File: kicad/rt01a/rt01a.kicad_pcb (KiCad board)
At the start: 4 copper layers, 90 x 66.3 mm, 75 parts, among them J1 Barrel_Jack_Switch, J10 Conn_01x07, J2 USB_C_Receptacle_USB2.0_14P, J3 Conn_01x07, J4 Conn_01x12, J5 Conn_01x12, J6 Conn_01x06, J7 Conn_01x02, J8 Conn_01x05, J9 Conn_01x04, Q1 DMP3099L, U1 R-78E5.0-1.0, U2 MCP73831-2-OT, U3 TLV75533PDBV, U4 MCP111T-xxxE_TT, U5 STM32L412R8Tx, U6 AT25SF081-SSHD-X, U7 RV-3028-C7

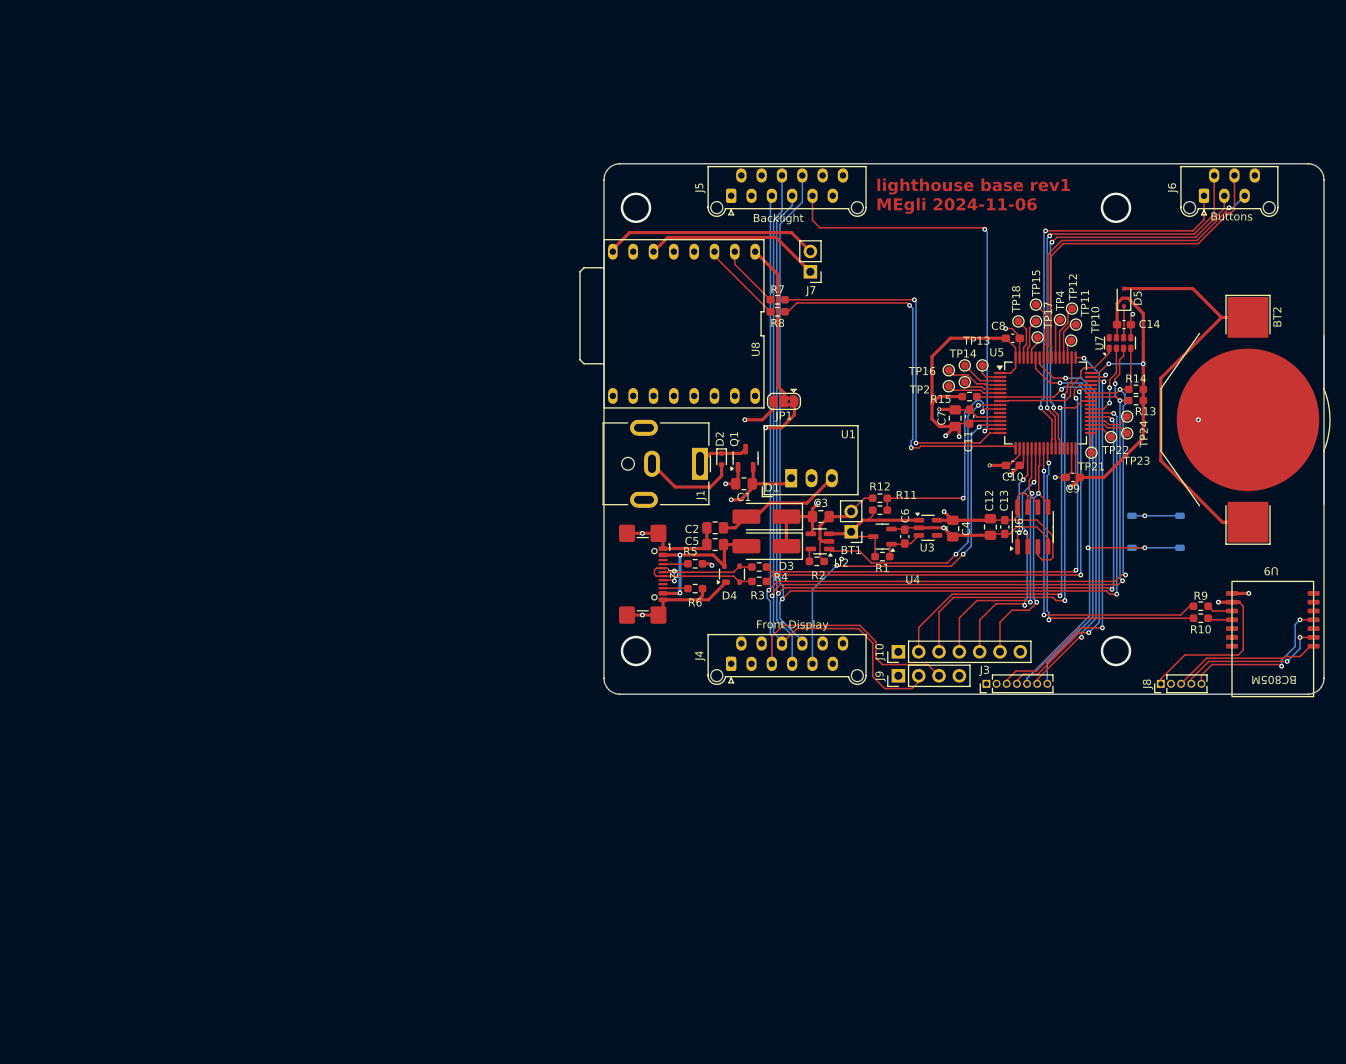
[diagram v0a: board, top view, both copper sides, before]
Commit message: rt01a added footprint, some placements done
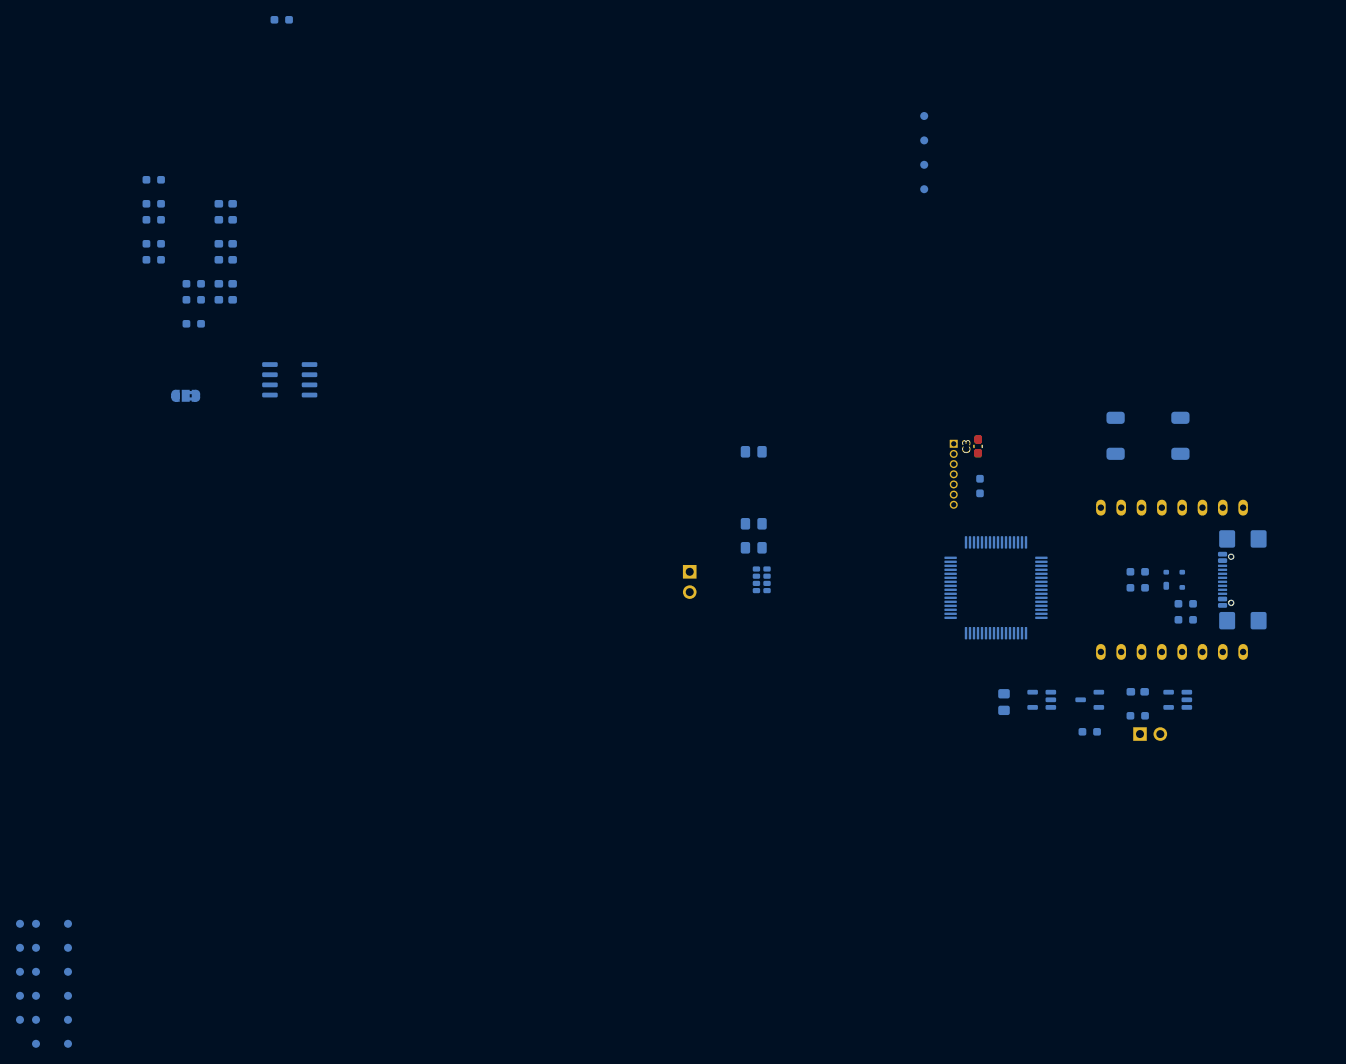
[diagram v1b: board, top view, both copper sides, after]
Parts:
- removed BT2: Keystone 3002, Battery:BatteryHolder_Keystone_3002_1x2032
- removed C13, C14: 100nF, Capacitor_SMD:C_0603_1608Metric_Pad1.08x0.95mm_HandSolder
- removed D2: DF2S16FS, Diode_SMD:D_SOD-523
- removed D3: B130-13-F, Diode_SMD:D_SMA_Handsoldering
- removed D4: PRTR5V0U2X, Package_TO_SOT_SMD:SOT-143
- removed D5: PMEG4002EJ, Diode_SMD:D_SOD-323F
- removed J10: Conn_01x07, Connector_PinHeader_2.54mm:PinHeader_1x07_P2.54mm_Vertical
- removed J2: USB_C_Receptacle_USB2.0_14P, Connector_USB:USB_C_Receptacle_GCT_USB4110
- removed J3: Conn_01x07, Connector_PinHeader_1.27mm:PinHeader_1x07_P1.27mm_Vertical
- removed J6: Conn_01x06, Connector_Molex:Molex_Picoflex_90325-0006_2x03_P1.27mm_Vertical
- removed J7: Conn_01x02, Connector_PinHeader_2.54mm:PinHeader_1x02_P2.54mm_Vertical
- removed J8: Conn_01x05, Connector_PinHeader_1.27mm:PinHeader_1x05_P1.27mm_Vertical
- removed J9: Conn_01x04, Connector_PinHeader_2.54mm:PinHeader_1x04_P2.54mm_Vertical
- removed Q1: DMP3099L, Package_TO_SOT_SMD:SOT-23-3
- removed TP22, TP23, TP24: TestPoint, TestPoint:TestPoint_Pad_D1.0mm
- removed U8: ~, lighthouse:DFPlayer_Mini-TF-16P
- removed U9: ~, lighthouse:BC805M
- added R16: 10k, Resistor_SMD:R_0603_1608Metric_Pad0.98x0.95mm_HandSolder, B.Cu at (-0.28, 30.0)
- added TP19: TestPoint, TestPoint:TestPoint_Pad_D1.0mm, B.Cu at (80.0, 45.1)
- added TP20: TestPoint, TestPoint:TestPoint_Pad_D1.0mm, B.Cu at (80.0, 48.1)
- added TP5: TestPoint, TestPoint:TestPoint_Pad_D1.0mm, B.Cu at (-27.0, 155.0)
- added TP6: TestPoint, TestPoint:TestPoint_Pad_D1.0mm, B.Cu at (-27.0, 158.0)
- added TP7: TestPoint, TestPoint:TestPoint_Pad_D1.0mm, B.Cu at (-31.0, 143.0)
- added TP8: TestPoint, TestPoint:TestPoint_Pad_D1.0mm, B.Cu at (-31.0, 146.0)
- added TP9: TestPoint, TestPoint:TestPoint_Pad_D1.0mm, B.Cu at (-31.0, 149.0)
- BT1, C1, C10, C2, C5, C8, C9, JP1, R1, R11, R12, R15, R2, R3, R4, R5, R6, R7, R8, TP1, TP10, TP11, TP12, TP13, TP14, TP15, TP16, TP17, TP18, TP2, TP21, TP3, TP4, U6, U7: moved to B.Cu
- C11: value 100nF -> 10uF; footprint Capacitor_SMD:C_0603_1608Metric_Pad1.08x0.95mm_HandSolder -> Capacitor_SMD:C_0805_2012Metric_Pad1.18x1.45mm_HandSolder; moved to B.Cu
- C12, C7: value 10uF -> 100nF; footprint Capacitor_SMD:C_0805_2012Metric_Pad1.18x1.45mm_HandSolder -> Capacitor_SMD:C_0603_1608Metric_Pad1.08x0.95mm_HandSolder; moved to B.Cu
- C3: value 10uF -> 10nF; footprint Capacitor_SMD:C_0805_2012Metric_Pad1.18x1.45mm_HandSolder -> Capacitor_SMD:C_0603_1608Metric_Pad1.08x0.95mm_HandSolder
- C4: value 10uF -> 10nF; footprint Capacitor_SMD:C_0805_2012Metric_Pad1.18x1.45mm_HandSolder -> Capacitor_SMD:C_0603_1608Metric_Pad1.08x0.95mm_HandSolder; moved to B.Cu
- C6: value 10nF -> 100nF; moved to B.Cu
- D1: value B130-13-F -> PRTR5V0U2X; footprint Diode_SMD:D_SMA_Handsoldering -> Package_TO_SOT_SMD:SOT-143; moved to B.Cu
- J1: value Barrel_Jack_Switch -> USB_C_Receptacle_USB2.0_14P; footprint Connector_BarrelJack:BarrelJack_CUI_PJ-063AH_Horizontal -> Connector_USB:USB_C_Receptacle_GCT_USB4110; moved to B.Cu
- J4: value Conn_01x12 -> Conn_01x07; footprint Connector_Molex:Molex_Picoflex_90325-0012_2x06_P1.27mm_Vertical -> Connector_PinHeader_1.27mm:PinHeader_1x07_P1.27mm_Vertical; moved to B.Cu
- J5: value Conn_01x12 -> Conn_01x02; footprint Connector_Molex:Molex_Picoflex_90325-0012_2x06_P1.27mm_Vertical -> Connector_PinHeader_2.54mm:PinHeader_1x02_P2.54mm_Vertical; moved to B.Cu
- R10, R9: value 0R -> 4k7; moved to B.Cu
- R13, R14: value 4k7 -> 0R; moved to B.Cu
- SW1: value ~ -> EVPBT3G4A000; footprint lighthouse:PTS526 -> rt:EVPBT3
- U1: value R-78E5.0-1.0 -> MCP73831-2-OT; footprint Converter_DCDC:Converter_DCDC_RECOM_R-78E-0.5_THT -> Package_TO_SOT_SMD:SOT-23-5; moved to B.Cu
- U2: value MCP73831-2-OT -> TLV75533PDBV; moved to B.Cu
- U3: value TLV75533PDBV -> MCP111T-xxxE_TT; footprint Package_TO_SOT_SMD:SOT-23-5 -> Package_TO_SOT_SMD:SOT-23-3; moved to B.Cu
- U4: value MCP111T-xxxE_TT -> STM32L412R8Tx; footprint Package_TO_SOT_SMD:SOT-23-3 -> Package_QFP:LQFP-64_10x10mm_P0.5mm; moved to B.Cu
- U5: value STM32L412R8Tx -> ~; footprint Package_QFP:LQFP-64_10x10mm_P0.5mm -> rt:DFPlayer_Mini-TF-16P; moved to B.Cu
- moved TP12 158.8 mm to (-31.0, 158.0), turned to 180 degrees
- moved TP11 156.4 mm to (-31.0, 155.0), turned to 180 degrees
- moved TP17 154.1 mm to (-33.0, 155.0), turned to 180 degrees
- moved TP10 153.1 mm to (-31.0, 152.0), turned to 180 degrees
- moved TP15 151.9 mm to (-33.0, 149.0), turned to 180 degrees
- moved TP4 150.1 mm to (-27.0, 152.0), turned to 180 degrees
- moved TP3 144.8 mm to (-27.0, 149.0), turned to 180 degrees
- moved R10 141.9 mm to (-16.3, 50.0)
- moved TP16 140.0 mm to (-33.0, 152.0), turned to 180 degrees
- moved TP13 139.1 mm to (-33.0, 143.0), turned to 180 degrees
- moved TP14 138.7 mm to (-33.0, 146.0), turned to 180 degrees
- moved TP1 131.0 mm to (-27.0, 143.0), turned to 180 degrees
- moved R9 130.7 mm to (-11.3, 68.0)
- moved TP2 130.6 mm to (-27.0, 146.0), turned to 180 degrees
- moved R13 124.3 mm to (-16.3, 58.0), turned to 180 degrees
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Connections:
- C1 pad 1: +12V -> VBUS
- C2 pad 1: Net-(D1-A) -> +3.3V
- C3 pad 1: +5V -> ~{STM_RST}
- C4 pad 1: +3.3V -> Net-(U2-EN)
- C5 pad 1: VBUS -> +3.3V
- C6 pad 1: Net-(U3-EN) -> +3.3V
- D1 pad 1: +5V -> GND
- D1 pad 2: Net-(D1-A) -> Net-(D1-I/O1)
- J4 pad 1: +12V -> +3.3V
- J4 pad 2: +5V -> GND
- J4 pad 3: +3.3V -> STM_SWDIO
- J4 pad 4: GND -> STM_SWDCLK
- J4 pad 5: I2C1_SDA -> ~{STM_RST}
- J4 pad 6: I2C1_SCL -> DBG_TX
- J4 pad 7: ~{IS_SDB} -> DBG_RX
- J5 pad 1: +12V -> Net-(J5-Pin_1)
- J5 pad 2: +5V -> Net-(J5-Pin_2)
- R1 pad 2: Net-(U3-EN) -> Net-(U2-EN)
- R10 pad 1: BLE_RX -> I2C1_SDA
- R10 pad 2: Net-(U5-PC5) -> +3.3V
- R11 pad 1: Net-(U5-PC2) -> Net-(U4-PC2)
- R12 pad 2: Net-(U5-PC2) -> Net-(U4-PC2)
- R13 pad 1: I2C1_SCL -> BLE_TX
- R13 pad 2: +3.3V -> Net-(U4-PC4)
- R14 pad 1: I2C1_SDA -> BLE_RX
- R14 pad 2: +3.3V -> Net-(U4-PC5)
- R2 pad 1: Net-(U2-PROG) -> Net-(U1-PROG)
- R3 pad 1: Net-(D4-I/O1) -> Net-(D1-I/O1)
- R4 pad 1: Net-(D4-I/O2) -> Net-(D1-I/O2)
- R5 pad 1: Net-(J2-CC1) -> Net-(J1-CC1)
- R6 pad 1: Net-(J2-CC2) -> Net-(J1-CC2)
- R7 pad 1: Net-(U5-PA2) -> Net-(U4-PA2)
- R8 pad 1: Net-(U5-PA3) -> Net-(U4-PA3)
- R9 pad 1: BLE_TX -> I2C1_SCL
- R9 pad 2: Net-(U5-PC4) -> +3.3V
- TP1 pad 1: Net-(U5-PH0) -> Net-(U4-PH0)
- TP10 pad 1: Net-(U5-PC10) -> Net-(U4-PB5)
- TP11 pad 1: Net-(U5-PC11) -> Net-(U4-PC15)
- TP12 pad 1: Net-(U5-PC12) -> Net-(U4-PB8)
- TP13 pad 1: Net-(U5-PC13) -> Net-(U4-PB9)
- TP14 pad 1: Net-(U5-PC14) -> Net-(U4-PB12)
- TP15 pad 1: Net-(U5-PB5) -> Net-(U4-PB13)
- TP16 pad 1: Net-(U5-PC15) -> Net-(U4-PB14)
- TP17 pad 1: Net-(U5-PB8) -> Net-(U4-PB15)
- TP18 pad 1: Net-(U5-PB9) -> +3.3V
- TP2 pad 1: Net-(U5-PH1) -> Net-(U4-PH1)
- TP21 pad 1: Net-(U5-PB12) -> GND
- TP3 pad 1: Net-(U5-PH3) -> Net-(U4-PH3)
- TP4 pad 1: Net-(U5-PD2) -> Net-(U4-PD2)
- U1 pad 1: +12V -> CH_STAT
- U1 pad 3: Net-(D1-A) -> +BATT
- U2 pad 1: CH_STAT -> +BATT
- U2 pad 3: +BATT -> Net-(U2-EN)
- U2 pad 4: +5V -> unconnected-(U2-NC-Pad4)
- U2 pad 5: Net-(U2-PROG) -> +3.3V
- U3 pad 1: +BATT -> Net-(U2-EN)
- U3 pad 3: Net-(U3-EN) -> +BATT
- U4 pad 1: Net-(U3-EN) -> +3.3V
- U4 pad 2: GND -> Net-(U4-PC13)
- U4 pad 3: +BATT -> Net-(U4-PC14)
- U5 pad 1: +3.3V -> Net-(JP1-C)
- U5 pad 10: Net-(U5-PC2) -> GND
- U5 pad 12: GND -> unconnected-(U5-ADKEY1-Pad12)
- U5 pad 13: +3.3V -> unconnected-(U5-ADKEY2-Pad13)
- U5 pad 14: WHITE_PWM1 -> unconnected-(U5-USBD+-Pad14)
- U5 pad 15: WHITE_PWM2 -> unconnected-(U5-USBD--Pad15)
- U5 pad 16: Net-(U5-PA2) -> unconnected-(U5-BUSY-Pad16)
- U5 pad 2: Net-(U5-PC13) -> SOUND_TX
- U5 pad 3: Net-(U5-PC14) -> SOUND_RX
- U5 pad 4: Net-(U5-PC15) -> unconnected-(U5-DAC_R-Pad4)
- U5 pad 5: Net-(U5-PH0) -> unconnected-(U5-DAC_L-Pad5)
- U5 pad 6: Net-(U5-PH1) -> Net-(J5-Pin_1)
- U5 pad 7: ~{STM_RST} -> GND
- U5 pad 8: RTC_CLK -> Net-(J5-Pin_2)
- U5 pad 9: CH_STAT -> unconnected-(U5-IO1-Pad9)
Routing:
- net +3.3V: track 338.6 -> 0.00 mm, vias 9 -> 0
- net I2C1_SDA: track 166.9 -> 0.00 mm, vias 3 -> 0
- net I2C1_SCL: track 163.8 -> 0.00 mm, vias 4 -> 0
- net ~{IS_INTB}: track 129.3 -> 0.00 mm, vias 3 -> 0
- net ~{IS_SDB}: track 126.9 -> 0.00 mm, vias 3 -> 0
- net GND: track 125.9 -> 0.00 mm, vias 15 -> 0
- net +5V: track 83.4 -> 0.00 mm, vias 2 -> 0
- net +12V: track 70.2 -> 0.00 mm, vias 1 -> 0
- net ~{STM_RST}: track 67.9 -> 0.00 mm, vias 3 -> 0
- net USB_D-: track 64.2 -> 0.00 mm, vias 2 -> 0
- net USB_D+: track 64.2 -> 0.00 mm, vias 2 -> 0
- net BTN1: track 53.7 -> 0.00 mm, vias 2 -> 0
- net WHITE_PWM2: track 52.5 -> 0.00 mm, vias 2 -> 0
- net ~{SPI1_CS2}: track 52.5 -> 0.00 mm, vias 2 -> 0
- net Net-(BT2-+): track 52.1 -> 0.00 mm
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- removed copper zone on In2.Cu, net GND
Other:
- board outline removed
- board text removed: "Backlight"
- board text removed: "Buttons"
- board text removed: "Front Display"
- board text removed: "lighthouse base rev1 MEgli 2024-11-06"

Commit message: schematics seems done
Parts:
- removed J4: Conn_01x07, Connector_PinHeader_1.27mm:PinHeader_1x07_P1.27mm_Vertical
- removed J5: Conn_01x02, Connector_PinHeader_2.54mm:PinHeader_1x02_P2.54mm_Vertical
- removed JP1: Jumper_3_Bridged12, Jumper:SolderJumper-3_P1.3mm_Bridged2Bar12_RoundedPad1.0x1.5mm
- removed TP17, TP18, TP19, TP20, TP21: TestPoint, TestPoint:TestPoint_Pad_D1.0mm
- added C13: 10uF, Capacitor_SMD:C_0805_2012Metric_Pad1.18x1.45mm_HandSolder, F.Cu at (247.5, 63.0)
- added C14: 100nF, Capacitor_SMD:C_0603_1608Metric_Pad1.08x0.95mm_HandSolder, F.Cu at (247.2, 52.7)
- added C15: 10nF, Capacitor_SMD:C_0603_1608Metric_Pad1.08x0.95mm_HandSolder, B.Cu at (162.5, 133.8)
- added C16: 10nF, Capacitor_SMD:C_0603_1608Metric_Pad1.08x0.95mm_HandSolder, B.Cu at (162.5, 136.3)
- added C17: 10nF, Capacitor_SMD:C_0603_1608Metric_Pad1.08x0.95mm_HandSolder, B.Cu at (162.5, 138.8)
- added C18: 10nF, Capacitor_SMD:C_0603_1608Metric_Pad1.08x0.95mm_HandSolder, B.Cu at (162.5, 141.3)
- added C19: 10nF, Capacitor_SMD:C_0603_1608Metric_Pad1.08x0.95mm_HandSolder, B.Cu at (162.5, 143.8)
- added C20: 100nF, Capacitor_SMD:C_0603_1608Metric_Pad1.08x0.95mm_HandSolder, B.Cu at (162.5, 146.3)
- added C21: 100nF, Capacitor_SMD:C_0603_1608Metric_Pad1.08x0.95mm_HandSolder, B.Cu at (162.5, 148.8)
- added C22: 10uF, Capacitor_SMD:C_0805_2012Metric_Pad1.18x1.45mm_HandSolder, B.Cu at (149.2, 154.1)
- added C23: 100nF, Capacitor_SMD:C_0603_1608Metric_Pad1.08x0.95mm_HandSolder, B.Cu at (158.1, 133.8)
- added D2: D_Schottky, Diode_SMD:D_SOD-523, B.Cu at (144.0, 154.0)
- added D3: ESD5Zxx, Diode_SMD:D_SMF, B.Cu at (148.7, 134.2)
- added D4: ESD5Zxx, Diode_SMD:D_SMF, B.Cu at (148.7, 137.6)
- added D5: ESD5Zxx, Diode_SMD:D_SMF, B.Cu at (148.7, 140.9)
- added D6: ESD5Zxx, Diode_SMD:D_SMF, B.Cu at (148.7, 144.2)
- added D7: ESD5Zxx, Diode_SMD:D_SMF, B.Cu at (148.7, 147.6)
- added D8: ESD5Zxx, Diode_SMD:D_SMF, B.Cu at (148.7, 150.9)
- added J2: Conn_01x07, Connector_PinHeader_1.27mm:PinHeader_1x07_P1.27mm_Vertical, F.Cu at (84.0, 83.0)
- added Q1: Q_NMOS_DGS, Package_TO_SOT_SMD:SOT-23-3, B.Cu at (143.2, 145.9)
- added Q2: Q_NMOS_DGS, Package_TO_SOT_SMD:SOT-23-3, B.Cu at (143.2, 150.6)
- added R17: 1M, Resistor_SMD:R_0603_1608Metric_Pad0.98x0.95mm_HandSolder, F.Cu at (247.2, 55.2)
- added R18: 10k, Resistor_SMD:R_0603_1608Metric_Pad0.98x0.95mm_HandSolder, F.Cu at (247.2, 57.7)
- added R19: 10k, Resistor_SMD:R_0603_1608Metric_Pad0.98x0.95mm_HandSolder, F.Cu at (247.2, 60.2)
- added R20: 10k, Resistor_SMD:R_0603_1608Metric_Pad0.98x0.95mm_HandSolder, B.Cu at (158.1, 136.3)
- added R21: 10k, Resistor_SMD:R_0603_1608Metric_Pad0.98x0.95mm_HandSolder, B.Cu at (158.1, 138.8)
- added R22: 10k, Resistor_SMD:R_0603_1608Metric_Pad0.98x0.95mm_HandSolder, B.Cu at (158.1, 141.3)
- added R23: 10k, Resistor_SMD:R_0603_1608Metric_Pad0.98x0.95mm_HandSolder, B.Cu at (158.1, 143.8)
- added R24: 10k, Resistor_SMD:R_0603_1608Metric_Pad0.98x0.95mm_HandSolder, B.Cu at (158.1, 146.3)
- added R25: 10k, Resistor_SMD:R_0603_1608Metric_Pad0.98x0.95mm_HandSolder, B.Cu at (158.1, 148.8)
- added R26: 10k, Resistor_SMD:R_0603_1608Metric_Pad0.98x0.95mm_HandSolder, B.Cu at (153.8, 133.8)
- added R27: 10k, Resistor_SMD:R_0603_1608Metric_Pad0.98x0.95mm_HandSolder, B.Cu at (153.8, 136.3)
- added R28: 10k, Resistor_SMD:R_0603_1608Metric_Pad0.98x0.95mm_HandSolder, B.Cu at (153.8, 138.8)
- added R29: 10k, Resistor_SMD:R_0603_1608Metric_Pad0.98x0.95mm_HandSolder, B.Cu at (153.8, 141.3)
- added U10: LTR-303ALS-01, OptoDevice:Lite-On_LTR-303ALS-01, B.Cu at (158.5, 152.0)
- added U11: LSM303C, Package_LGA:LGA-12_2x2mm_P0.5mm, B.Cu at (154.4, 152.1)
- added U8: GC9A01, rt:FP-128HR01A, F.Cu at (100.0, 108.8)
- added U9: SHTC3, Sensor_Humidity:Sensirion_DFN-4-1EP_2x2mm_P1mm_EP0.7x1.6mm, B.Cu at (162.4, 151.9)
- C10, C12: value 100nF -> 10nF
- C2, C5: value 10uF -> 100nF; footprint Capacitor_SMD:C_0805_2012Metric_Pad1.18x1.45mm_HandSolder -> Capacitor_SMD:C_0603_1608Metric_Pad1.08x0.95mm_HandSolder
- C3, C4: value 10nF -> 100nF
- C7, C9: value 100nF -> 10uF; footprint Capacitor_SMD:C_0603_1608Metric_Pad1.08x0.95mm_HandSolder -> Capacitor_SMD:C_0805_2012Metric_Pad1.18x1.45mm_HandSolder
- R10: value 4k7 -> 10k
- R11, R12: value 1M -> 4k7
- R13, R14: value 0R -> 1M
- R15: value 10k -> 10R
- R2: value 10k -> 1M
- R3, R4: value 22R -> 5k1
- R5: value 5k1 -> 10k
- R6: value 5k1 -> 22R
- R7: value 0R -> 22R
- R9: value 4k7 -> 0R
- U1: value MCP73831-2-OT -> RV-3028-C7; footprint Package_TO_SOT_SMD:SOT-23-5 -> Package_SON:MicroCrystal_C7_SON-8_1.5x3.2mm_P0.9mm
- U2: value TLV75533PDBV -> STM32L412R8Tx; footprint Package_TO_SOT_SMD:SOT-23-5 -> Package_QFP:LQFP-64_10x10mm_P0.5mm
- U3: value MCP111T-xxxE_TT -> MCP73831-2-OT; footprint Package_TO_SOT_SMD:SOT-23-3 -> Package_TO_SOT_SMD:SOT-23-5
- U4: value STM32L412R8Tx -> AT25SF081-SSHD-X; footprint Package_QFP:LQFP-64_10x10mm_P0.5mm -> Package_SO:SOIC-8_3.9x4.9mm_P1.27mm
- U5: value ~ -> MCP111T-xxxE_TT; footprint rt:DFPlayer_Mini-TF-16P -> Package_TO_SOT_SMD:SOT-23-3
- U6: value AT25SF081-SSHD-X -> TLV75533PDBV; footprint Package_SO:SOIC-8_3.9x4.9mm_P1.27mm -> Package_TO_SOT_SMD:SOT-23-5
- U7: value RV-3028-C7 -> ~; footprint Package_SON:MicroCrystal_C7_SON-8_1.5x3.2mm_P0.9mm -> rt:DFPlayer_Mini-TF-16P_Minimal
- moved TP1 189.3 mm to (154.0, 87.5)
- moved TP10 189.3 mm to (150.0, 96.5)
- moved TP11 189.3 mm to (150.0, 99.5)
- moved TP12 189.3 mm to (150.0, 102.5)
- moved TP13 189.3 mm to (148.0, 87.5)
- moved TP14 189.3 mm to (148.0, 90.5)
- moved TP15 189.3 mm to (148.0, 93.5)
- moved TP16 189.3 mm to (148.0, 96.5)
- moved TP2 189.3 mm to (154.0, 90.5)
- moved TP3 189.3 mm to (154.0, 93.5)
- moved TP4 189.3 mm to (154.0, 96.5)
- moved TP5 189.3 mm to (154.0, 99.5)
- moved TP6 189.3 mm to (154.0, 102.5)
- moved TP7 189.3 mm to (150.0, 87.5)
- moved TP8 189.3 mm to (150.0, 90.5)
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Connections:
- C1 pad 1: VBUS -> +3.3V
- C10 pad 1: +3.3V -> Net-(U5-VOUT)
- C12 pad 1: +3.3V -> ~{STM_RST}
- C3 pad 1: ~{STM_RST} -> +3.3V
- C4 pad 1: Net-(U2-EN) -> +3.3V
- C7 pad 1: +3.3V -> VBUS
- R1 pad 1: +BATT -> Net-(U2-PC2)
- R1 pad 2: Net-(U2-EN) -> +BATT
- R10 pad 1: I2C1_SDA -> Net-(U3-PROG)
- R10 pad 2: +3.3V -> GND
- R11 pad 1: Net-(U4-PC2) -> I2C1_SCL
- R11 pad 2: +BATT -> +3.3V
- R12 pad 1: GND -> I2C1_SDA
- R12 pad 2: Net-(U4-PC2) -> +3.3V
- R13 pad 1: BLE_TX -> +BATT
- R13 pad 2: Net-(U4-PC4) -> Net-(U5-VOUT)
- R14 pad 1: BLE_RX -> DISP_BG
- R14 pad 2: Net-(U4-PC5) -> GND
- R15 pad 1: ~{STM_RST} -> Net-(U8-LEDK)
- R15 pad 2: +3.3V -> Net-(Q1-D)
- R16 pad 1: GND -> ~{STM_RST}
- R16 pad 2: Net-(U7-VBACKUP) -> +3.3V
- R2 pad 1: Net-(U1-PROG) -> GND
- R2 pad 2: GND -> Net-(U2-PC2)
- R3 pad 1: Net-(D1-I/O1) -> Net-(J1-CC1)
- R3 pad 2: USB_D- -> GND
- R4 pad 1: Net-(D1-I/O2) -> Net-(J1-CC2)
- R4 pad 2: USB_D+ -> GND
- R5 pad 1: Net-(J1-CC1) -> GND
- R5 pad 2: GND -> Net-(U1-VBACKUP)
- R6 pad 1: Net-(J1-CC2) -> Net-(D1-I/O1)
- R6 pad 2: GND -> USB_D-
- R7 pad 1: Net-(U4-PA2) -> Net-(D1-I/O2)
- R7 pad 2: SOUND_TX -> USB_D+
- R8 pad 1: Net-(U4-PA3) -> Net-(U2-PA2)
- R8 pad 2: SOUND_RX -> SOUND_TX
- R9 pad 1: I2C1_SCL -> Net-(U2-PA3)
- R9 pad 2: +3.3V -> SOUND_RX
- TP1 pad 1: Net-(U4-PH0) -> +3.3V
- TP10 pad 1: Net-(U4-PB5) -> Net-(D6-K)
- TP11 pad 1: Net-(U4-PC15) -> GND
- TP12 pad 1: Net-(U4-PB8) -> Net-(D5-K)
- TP13 pad 1: Net-(U4-PB9) -> GND
- TP14 pad 1: Net-(U4-PB12) -> +3.3V
- TP15 pad 1: Net-(U4-PB13) -> Net-(D2-A)
- TP16 pad 1: Net-(U4-PB14) -> Net-(U2-PB15)
- TP2 pad 1: Net-(U4-PH1) -> GND
- TP3 pad 1: Net-(U4-PH3) -> I2C1_SCL
- TP4 pad 1: Net-(U4-PD2) -> I2C1_SDA
- TP5 pad 1: Net-(U4-PC10) -> Net-(D3-K)
- TP6 pad 1: Net-(U4-PC11) -> Net-(D4-K)
- TP7 pad 1: Net-(U4-PC12) -> GND
- TP8 pad 1: Net-(U4-PC13) -> Net-(D7-K)
- TP9 pad 1: Net-(U4-PC14) -> GND
- U1 pad 1: CH_STAT -> RTC_CLK
- U1 pad 2: GND -> RTC_INT
- U1 pad 3: +BATT -> I2C1_SCL
- U1 pad 4: VBUS -> I2C1_SDA
- U1 pad 5: Net-(U1-PROG) -> GND
- U2 pad 1: +BATT -> +3.3V
- U2 pad 2: GND -> unconnected-(U2-PC13-Pad2)
- U2 pad 3: Net-(U2-EN) -> unconnected-(U2-PC14-Pad3)
- U2 pad 5: +3.3V -> unconnected-(U2-PH0-Pad5)
- U3 pad 1: Net-(U2-EN) -> CH_STAT
- U4 pad 1: +3.3V -> ~{SPI1_CS}
- U4 pad 2: Net-(U4-PC13) -> SPI1_CIPO
- U4 pad 3: Net-(U4-PC14) -> +3.3V
- U4 pad 4: Net-(U4-PC15) -> GND
- U4 pad 5: Net-(U4-PH0) -> SPI1_COPI
- U4 pad 6: Net-(U4-PH1) -> SPI1_SCLK
- U4 pad 7: ~{STM_RST} -> +3.3V
- U4 pad 8: RTC_CLK -> +3.3V
- U5 pad 1: Net-(JP1-C) -> Net-(U5-VOUT)
- U5 pad 2: SOUND_TX -> GND
- U5 pad 3: SOUND_RX -> +BATT
- U6 pad 1: ~{SPI1_CS} -> +BATT
- U6 pad 2: SPI1_CIPO -> GND
- U6 pad 3: +3.3V -> Net-(U5-VOUT)
- U6 pad 4: GND -> unconnected-(U6-NC-Pad4)
- U6 pad 5: SPI1_COPI -> +3.3V
- U7 pad 1: RTC_CLK -> +3.3V
- U7 pad 2: ~{RTC_INT} -> SOUND_TX
- U7 pad 3: I2C1_SCL -> SOUND_RX
- U7 pad 7: +3.3V -> GND
